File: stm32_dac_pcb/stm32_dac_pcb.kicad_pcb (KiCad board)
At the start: 2 copper layers, 64.3 x 21.8 mm, 42 parts, among them J201 Conn_01x03, J202 Conn_01x05, J301 AudioJack4, P201 USB_C_Plug_USB2.0, SW201 SW_Push, SW202 SW_Push, SW203 SW_Push, U101 AP1117-33, U102 AP1117-33, U201 STM32F411CEUx, U301 PCM5102A

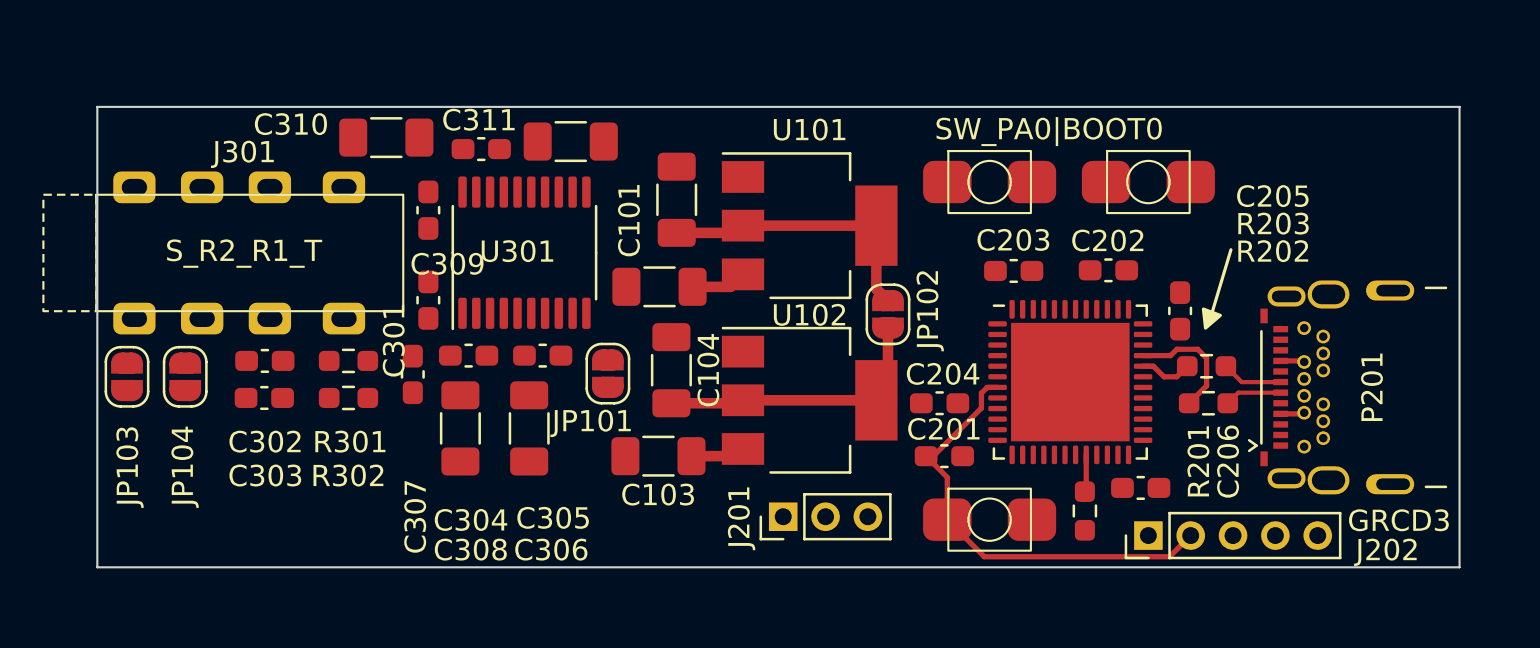
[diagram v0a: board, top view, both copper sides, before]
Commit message: Clean up tantalum capacitors
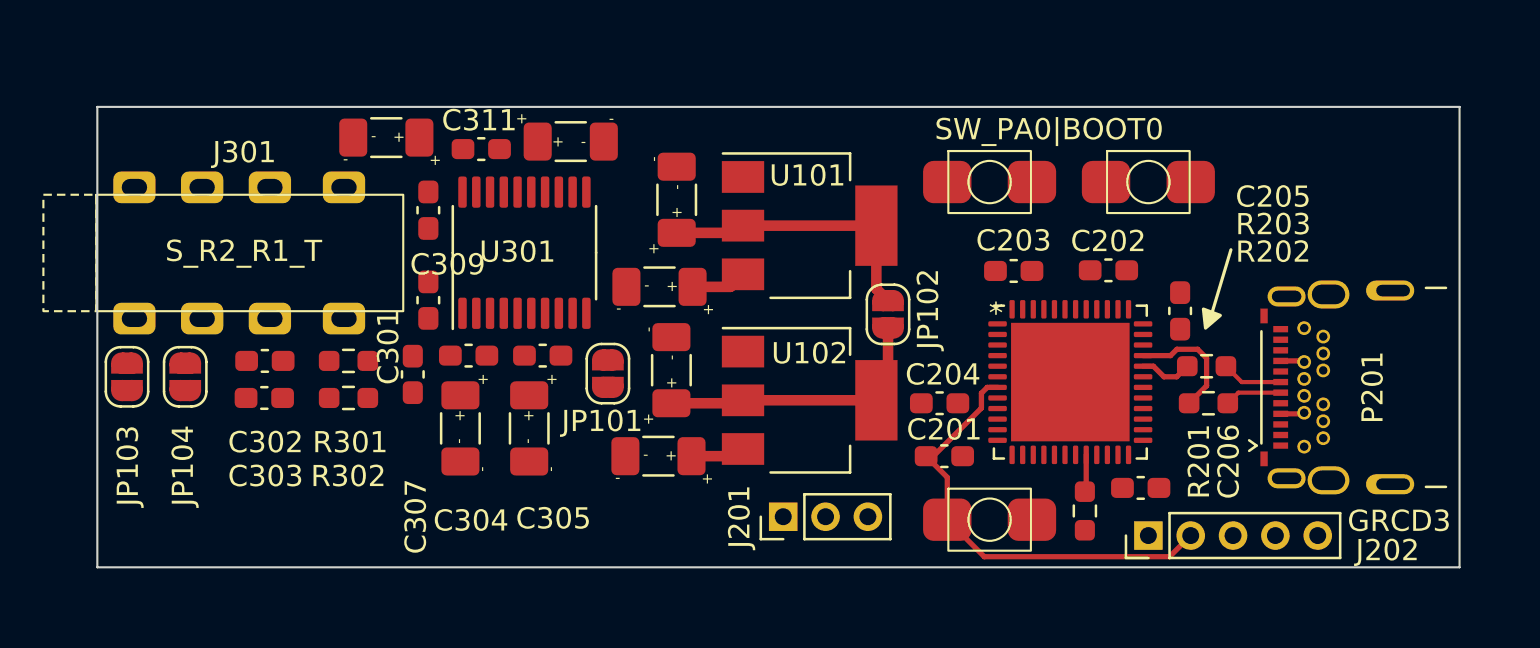
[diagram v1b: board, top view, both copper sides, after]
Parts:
- C101, C102, C103, C104, C306, C308, C310, C312: footprint Capacitor_SMD:C_1206_3216Metric_Pad1.33x1.80mm_HandSolder -> 0_project_fp_lib:C_1206_3216Metric_Pad1.33x1.80mm_HandSolder_Polar
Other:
- board text added: "*"

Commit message: Mostly finish up
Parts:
- removed JP101: SolderJumper_2_Open, Jumper:SolderJumper-2_P1.3mm_Open_RoundedPad1.0x1.5mm
- added C207: 2.2u, Capacitor_SMD:C_0603_1608Metric_Pad1.08x0.95mm_HandSolder, F.Cu at (123.3, 104.7)
- added H101: MountingHole, MountingHole:MountingHole_2.2mm_M2, F.Cu at (98.7, 104.1)
- added H102: MountingHole, MountingHole:MountingHole_2.2mm_M2, F.Cu at (153.9, 87.8)
- added J203: Conn_01x01, Connector_PinHeader_2.00mm:PinHeader_1x01_P2.00mm_Vertical, F.Cu at (158.0, 88.1)
- added R204: 5.1k, Resistor_SMD:R_0603_1608Metric_Pad0.98x0.95mm_HandSolder, F.Cu at (155.7, 91.8)
- moved C205 1.05 mm to (147.0, 93.8)
- moved C204 0.29 mm to (135.7, 99.0), turned to 90 degrees
- moved R202 0.25 mm to (148.3, 99.0)
- moved C304 0.10 mm to (113.4, 97.1)
- moved R201 0.10 mm to (142.4, 104.3)
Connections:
- C101 pad 2: GNDA -> GND
- C102 pad 2: GNDA -> GND
- C302 pad 2: GNDA -> GND
- C303 pad 2: GNDA -> GND
- C304 pad 2: GNDA -> GND
- C305 pad 2: GNDA -> GND
- C306 pad 2: GNDA -> GND
- C307 pad 2: GNDA -> GND
- C308 pad 2: GNDA -> GND
- J301 pad R2: GNDA -> GND
- P201 pad A5: /microcontroller_sheet/USB_CC -> Net-(P201-CC)
- P201 pad B5: unconnected-(P201-VCONN-PadB5) -> Net-(J203-Pin_1)
- U101 pad 1: GNDA -> GND
- U201 pad 22: unconnected-(U201-VCAP1-Pad22) -> Net-(U201-VCAP1)
- U301 pad 3: GNDA -> GND
- U301 pad 9: GNDA -> GND
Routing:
- net GND: track 0.00 -> 95.4 mm, vias 0 -> 13
- net +3.3V: track 13.4 -> 105.6 mm, vias 0 -> 4
- net /microcontroller_sheet/MIC_IN_1: track 0.00 -> 51.3 mm, vias 0 -> 2
- net +5V: track 7.46 -> 57.3 mm, vias 0 -> 4
- net /microcontroller_sheet/MIC_IN_2: track 0.00 -> 44.7 mm, vias 0 -> 2
- net /dac_sheet/MUTE_CONTROL: track 0.00 -> 40.2 mm, vias 0 -> 2
- net /dac_sheet/LRCK: track 0.00 -> 40.0 mm, vias 0 -> 2
- net /dac_sheet/BCK: track 0.00 -> 39.1 mm, vias 0 -> 2
- net /dac_sheet/DIN: track 0.00 -> 37.3 mm, vias 0 -> 2
- net Net-(U201-PA0): track 0.00 -> 28.3 mm, vias 0 -> 4
- net +3.3VA: track 13.3 -> 37.3 mm
- net Net-(U201-VCAP1): track 0.00 -> 23.9 mm, vias 0 -> 2
- net /microcontroller_sheet/NRST: track 21.2 -> 40.2 mm, vias 0 -> 2
- net Net-(C303-Pad1): track 0.00 -> 16.6 mm
- net /microcontroller_sheet/SWCLK: track 0.00 -> 16.3 mm, vias 0 -> 1
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- added copper zone on B.Cu, net GND
- added copper zone on F.Cu, net GND
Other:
- board text added: "A"
- board text added: "D"
- board text added: "G_TX_RX"
- board text added: "No 1206 caps are labelled with ref's. All labels are for 0603 parts only."
- board text added: "Rev1 2023-12-26 STM32 DAC DeflateAwning"
- board text added: "Top+Bottom GND Plane"

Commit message: Small updates
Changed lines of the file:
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@@
   (segment (start 140.5625 102.17474) (end 140.5625 101.6875) (width 0.25) (layer "F.Cu") (net 52))
   (segment (start 139.983002 102.45) (end 140.28724 102.45) (width 0.25) (layer "F.Cu") (net 52))
+  (segment (start 104.1 101.8) (end 103.8 101.5) (width 0.25) (layer "F.Cu") (net 52))
   (segment (start 139.5 102.7755) (end 139.657502 102.7755) (width 0.25) (layer "F.Cu") (net 52))
   (segment (start 140.28724 102.45) (end 140.5625 102.17474) (width 0.25) (layer "F.Cu") (net 52))
-  (segment (start 100.4 101.8) (end 97.25 98.65) (width 0.25) (layer "F.Cu") (net 52))
-  (segment (start 104.1 101.8) (end 100.4 101.8) (width 0.25) (layer "F.Cu") (net 52))
+  (segment (start 103.8 101.5) (end 100.1 101.5) (width 0.25) (layer "F.Cu") (net 52))
+  (segment (start 100.1 101.5) (end 97.25 98.65) (width 0.25) (layer "F.Cu") (net 52))
   (segment (start 139.657502 102.7755) (end 139.983002 102.45) (width 0.25) (layer "F.Cu") (net 52))
   (via (at 104.1 101.8) (size 0.8) (drill 0.4) (layers "F.Cu" "B.Cu") (net 52))

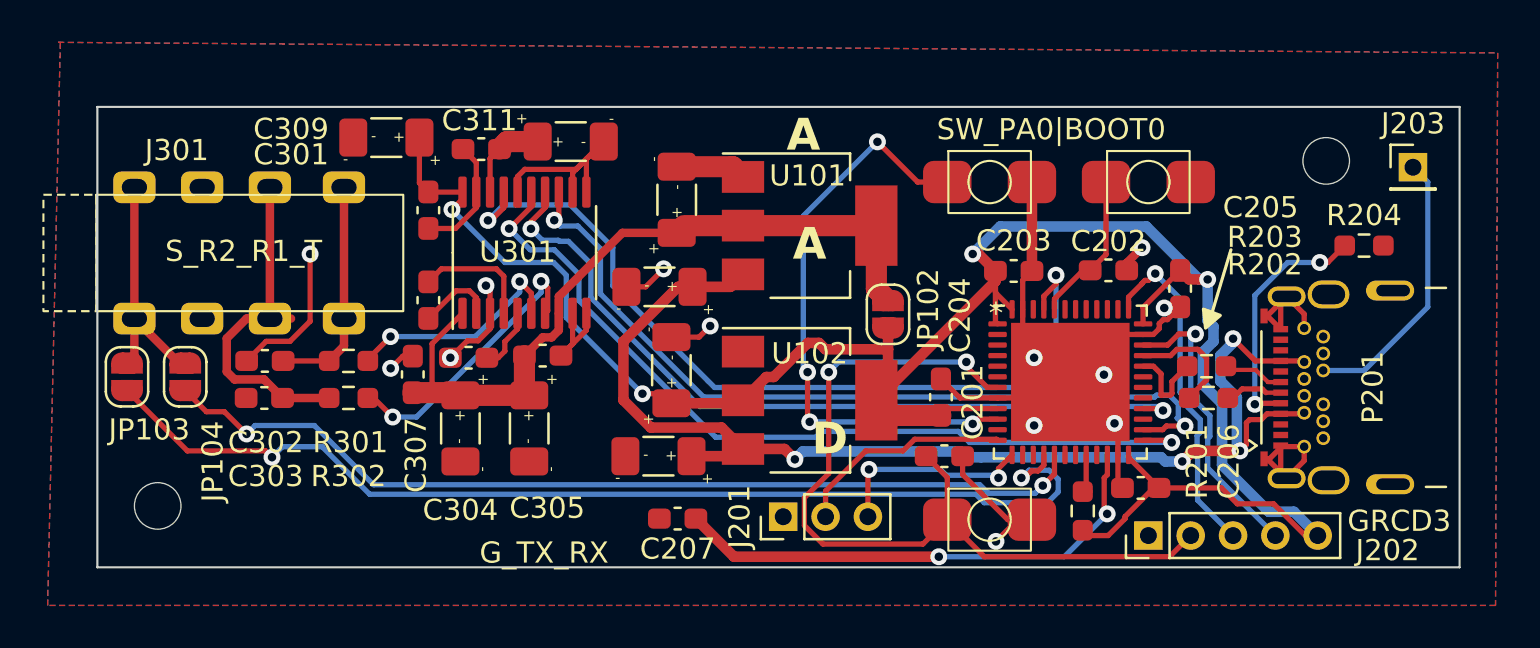
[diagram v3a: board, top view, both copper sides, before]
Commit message: Fix USB connector, finish routing, export rev1 gerber
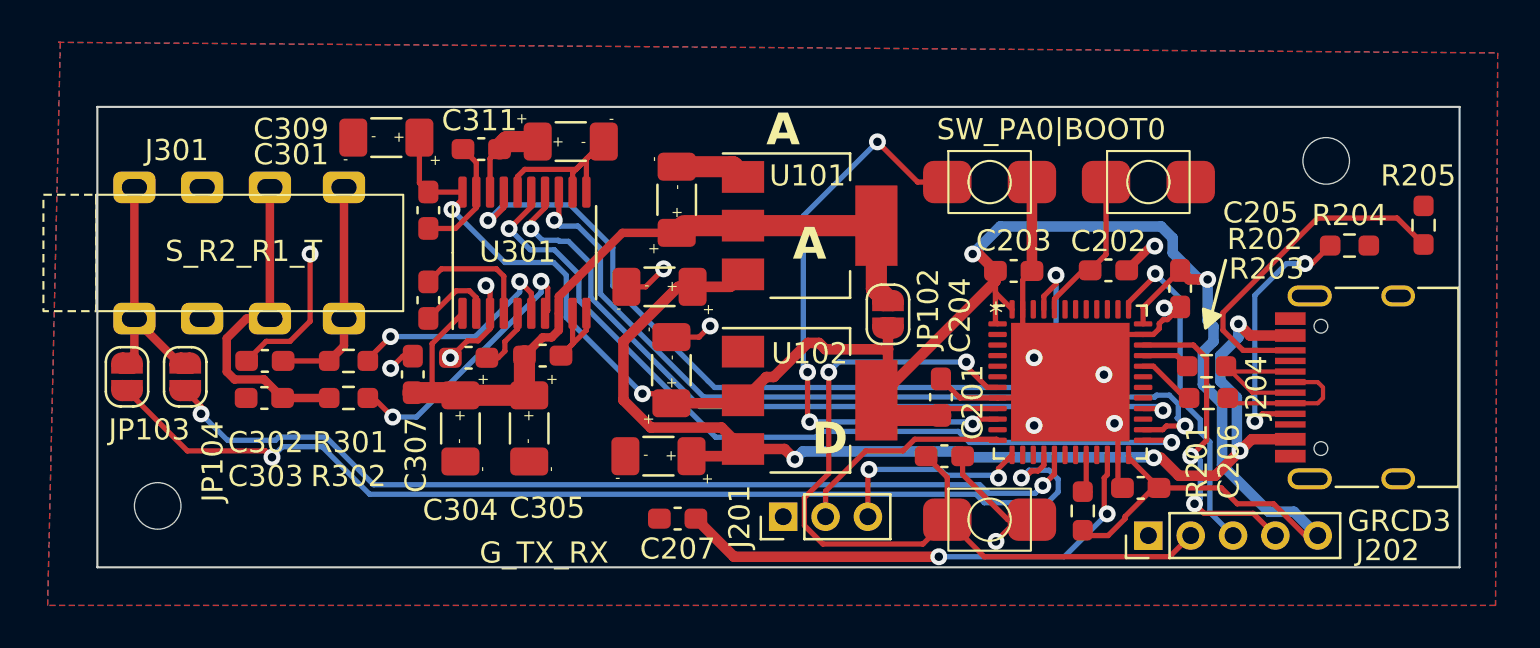
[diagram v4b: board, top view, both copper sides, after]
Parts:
- removed J203: Conn_01x01, Connector_PinHeader_2.00mm:PinHeader_1x01_P2.00mm_Vertical
- removed P201: USB_C_Plug_USB2.0, Connector_USB:USB_C_Receptacle_CNCTech_C-ARA1-AK51X
- added J204: USB_C_Receptacle_USB2.0, Connector_USB:USB_C_Receptacle_HRO_TYPE-C-31-M-12, F.Cu at (156.2, 98.5)
- added R205: 5.1k, Resistor_SMD:R_0603_1608Metric_Pad0.98x0.95mm_HandSolder, F.Cu at (158.5, 90.8)
- moved R202 1.50 mm to (148.2, 97.5)
- moved R203 1.50 mm to (148.3, 99.0)
- moved R204 0.69 mm to (155.0, 91.8)
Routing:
- net Net-(J204-CC2): track 0.00 -> 16.2 mm
- net Net-(J203-Pin_1): track 13.1 -> 0.00 mm
- net GND: track 95.4 -> 82.7 mm
- net /microcontroller_sheet/USB_DN: track 2.90 -> 6.86 mm
- net /microcontroller_sheet/USB_DP: track 2.85 -> 6.71 mm
- net Net-(U201-PA12): track 5.52 -> 2.29 mm
- net +5V: track 57.3 -> 55.7 mm
- net Net-(U201-PA11): track 4.14 -> 2.80 mm
- net /microcontroller_sheet/SWDIO: track 14.1 -> 15.3 mm, vias 1 -> 2
- net Net-(C303-Pad1): track 16.6 -> 15.6 mm
- net Net-(J204-CC1): track 11.6 -> 12.3 mm
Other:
- board text added: "1206 caps are not labelled with reference designators (all are the same model). All labels are for 0603 parts only."
- board text added: "Rev 1 2024-01-01 STM32 DAC DeflateAwning"
- board text removed: "No 1206 caps are labelled with ref's. All labels are for 0603 parts only."
- board text removed: "Rev1 2023-12-26 STM32 DAC DeflateAwning"

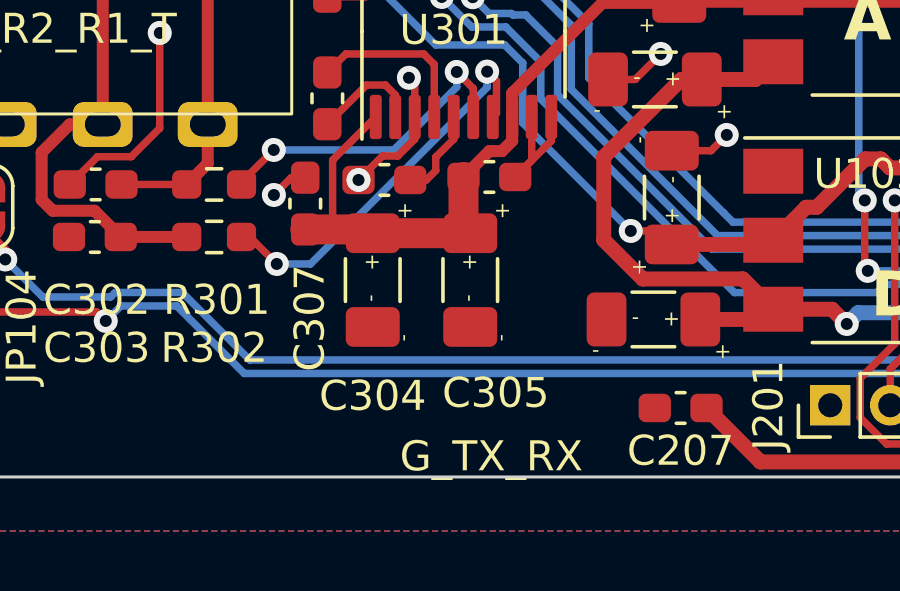
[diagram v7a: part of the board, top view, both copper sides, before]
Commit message: Schematic: Add 100u cap, fix BOOT0
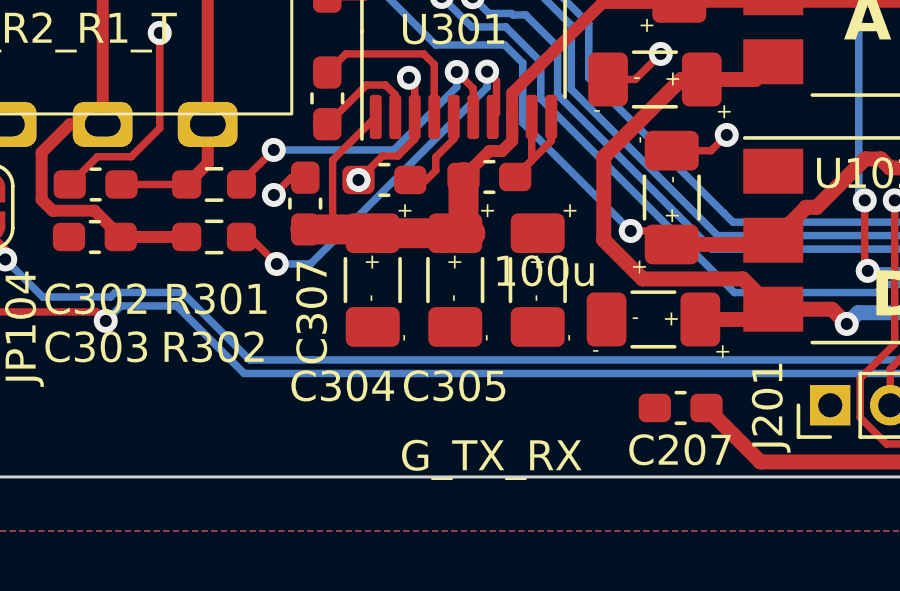
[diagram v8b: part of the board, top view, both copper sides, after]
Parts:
- added C313: 100u, 0_project_fp_lib:C_1206_3216Metric_Pad1.33x1.80mm_HandSolder_Polar, F.Cu at (118.5, 100.4)
- moved C306 0.50 mm to (115.8, 100.4)
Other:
- board text added: "100u"
